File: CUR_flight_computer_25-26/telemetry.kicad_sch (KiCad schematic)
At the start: 8 parts, among them J14 Conn_Coaxial_Small, U5 E22-400M30S

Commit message: finished footprints
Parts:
- J14: footprint Connector_Coxaial_RFSOLUTIONS_CON-SMA-EDGE-S:Connector_Coxaial_RFSOLUTIONS_CON-SMA-EDGE-S -> Connector_Coxaial_RFSOLUTIONS_CON-SMA-EDGE-S:Conn_Coaxial_RFSOLUTIONS_CON-SMA-EDGE-S
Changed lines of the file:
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@@
 			)
 		)
-		(property "Footprint" "Connector_Coxaial_RFSOLUTIONS_CON-SMA-EDGE-S:Connector_Coxaial_RFSOLUTIONS_CON-SMA-EDGE-S"
+		(property "Footprint" "Connector_Coxaial_RFSOLUTIONS_CON-SMA-EDGE-S:Conn_Coaxial_RFSOLUTIONS_CON-SMA-EDGE-S"
 			(at 128.27 45.72 0)
 			(effects

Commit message: most of layout figured out
trouble finding room for power
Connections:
- net +3.3V is gone; now on net +3V3: R7.1
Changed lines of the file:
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@@
+	)
+	(symbol
+		(lib_id "power:+3V3")
+		(at 44.45 52.07 0)
+		(unit 1)
+		(exclude_from_sim no)
+		(in_bom yes)
+		(on_board yes)
+		(dnp no)
+		(fields_autoplaced yes)
+		(property "Reference" "#PWR044"
+			(at 44.45 55.88 0)
+			(effects
+				(font
+					(size 1.27 1.27)
+				)
+				(hide yes)
+			)
+		)
+		(property "Value" "+3V3"
+			(at 44.45 46.99 0)
+			(effects
+				(font
+					(size 1.27 1.27)
+				)
+			)
+		)
+		(property "Footprint" ""
+			(at 44.45 52.07 0)
+			(effects
+				(font
+					(size 1.27 1.27)
+				)
+				(hide yes)
+			)
+		)
+		(property "Datasheet" ""
+			(at 44.45 52.07 0)
+			(effects
+				(font
+					(size 1.27 1.27)
+				)
+				(hide yes)
+			)
+		)
+		(property "Description" "Power symbol creates a global label with name \"+3V3\""
+			(at 44.45 52.07 0)
+			(effects
+				(font
+					(size 1.27 1.27)
+				)
+				(hide yes)
+			)
+		)
+		(pin "1"
+		)
+		(instances
+			(project "CUR_flight_computer_25-26"
+				(path "/bf7761cc-1b32-4d86-809c-5f027005229b/16b7f3d3-745f-44d9-93a4-41f5bfd830cb"
+					(reference "#PWR044")
+					(unit 1)
+				)
+			)
+		)
 	)
 	(symbol
@@
 					(unit 1)
 				)
-			)
-		)
-	)
-	(symbol
-		(lib_id "power:+3.3V")
-		(at 44.45 52.07 0)
-		(unit 1)
-		(exclude_from_sim no)
-		(in_bom yes)
-		(on_board yes)
-		(dnp no)
-		(fields_autoplaced yes)
-		(property "Reference" "#PWR044"
-			(at 44.45 55.88 0)
-			(effects
-				(font
-					(size 1.27 1.27)
-				)
-				(hide yes)
-			)
-		)
-		(property "Value" "+3.3V"
-			(at 44.45 46.99 0)
-			(effects
-				(font
-					(size 1.27 1.27)
-				)
-			)
-		)
-		(property "Footprint" ""
-			(at 44.45 52.07 0)
-			(effects
-				(font
-					(size 1.27 1.27)
-				)
-				(hide yes)
-			)
-		)
-		(property "Datasheet" ""
-			(at 44.45 52.07 0)
-			(effects
-				(font
-					(size 1.27 1.27)
-				)
-				(hide yes)
-			)
-		)
-		(property "Description" "Power symbol creates a global label with name \"+3.3V\""
-			(at 44.45 52.07 0)
-			(effects
-				(font
-					(size 1.27 1.27)
-				)
-				(hide yes)
-			)
-		)
-		(pin "1"
-		)
-		(instances
-			(project "CUR_flight_computer_25-26"
-				(path "/bf7761cc-1b32-4d86-809c-5f027005229b/16b7f3d3-745f-44d9-93a4-41f5bfd830cb"
-					(reference "#PWR044")
-					(unit 1)
-				)

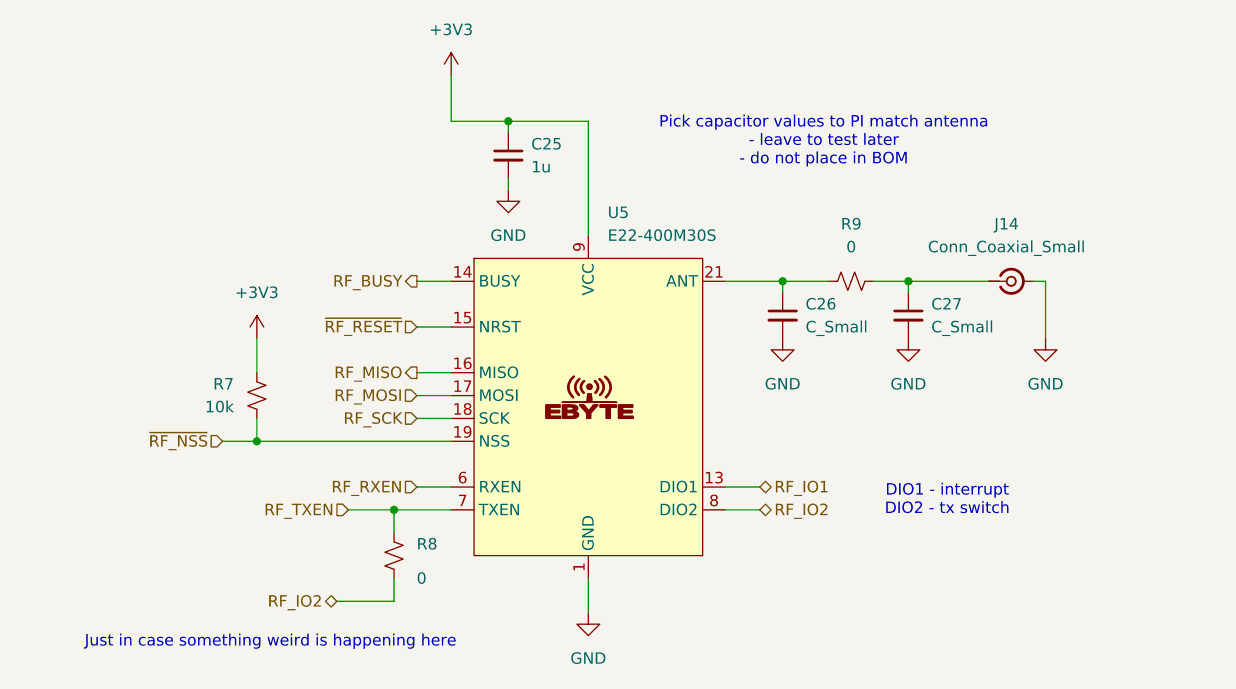
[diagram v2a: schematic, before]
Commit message: added testpoints to schematic
need to update layout
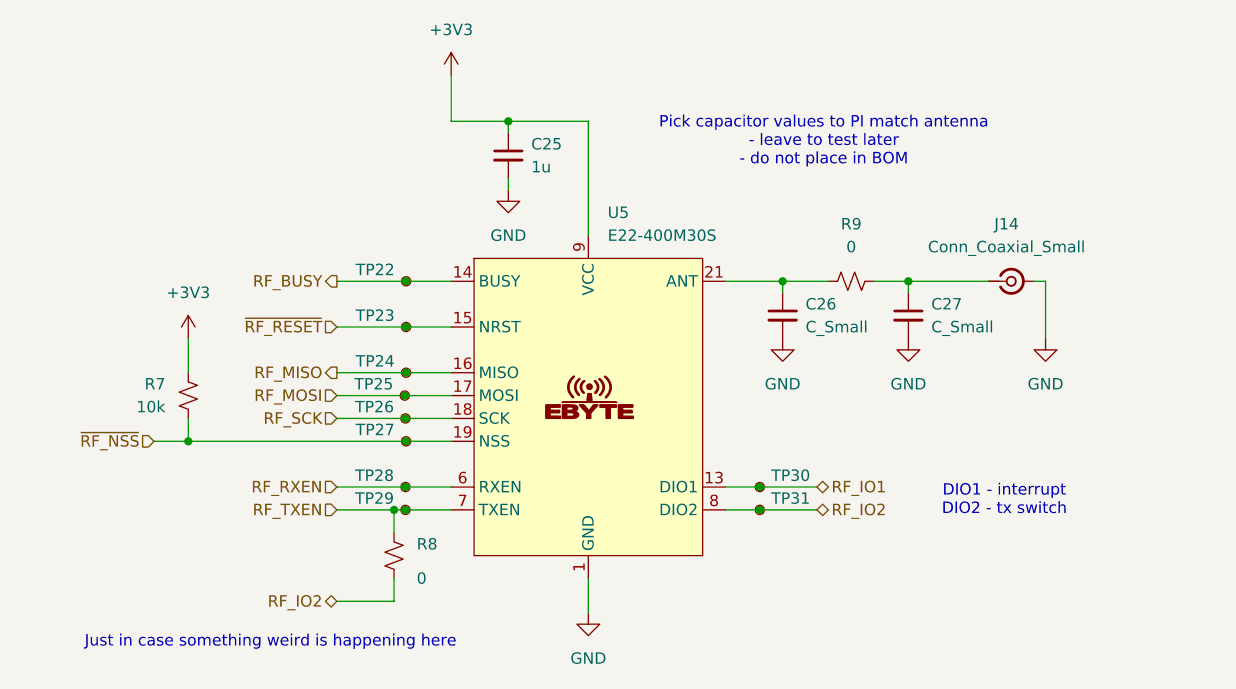
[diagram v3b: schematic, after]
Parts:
- added TP22, TP23, TP24, TP25, TP26, TP27, TP28, TP29, TP30, TP31: TestPoint_Small, TestPoint_KOASpeer:TestPoint_Chip_RCUCTE_0603, symbol Connector:TestPoint_Small
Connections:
- net RF_BUSY: now also TP22.1
- net RF_IO1: now also TP30.1
- net RF_IO2: now also TP31.1
- net RF_MISO: now also TP24.1
- net RF_MOSI: now also TP25.1
- net RF_RXEN: now also TP28.1
- net RF_SCK: now also TP26.1
- net RF_TXEN: now also TP29.1
- net ~{RF_NSS}: now also TP27.1
- net ~{RF_RESET}: now also TP23.1
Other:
- moved on the sheet: R7

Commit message: updated rf module to ebyte-lora-400MM-22s
added footprint
added symbol
updates schematic
updated pcb
need to reroute
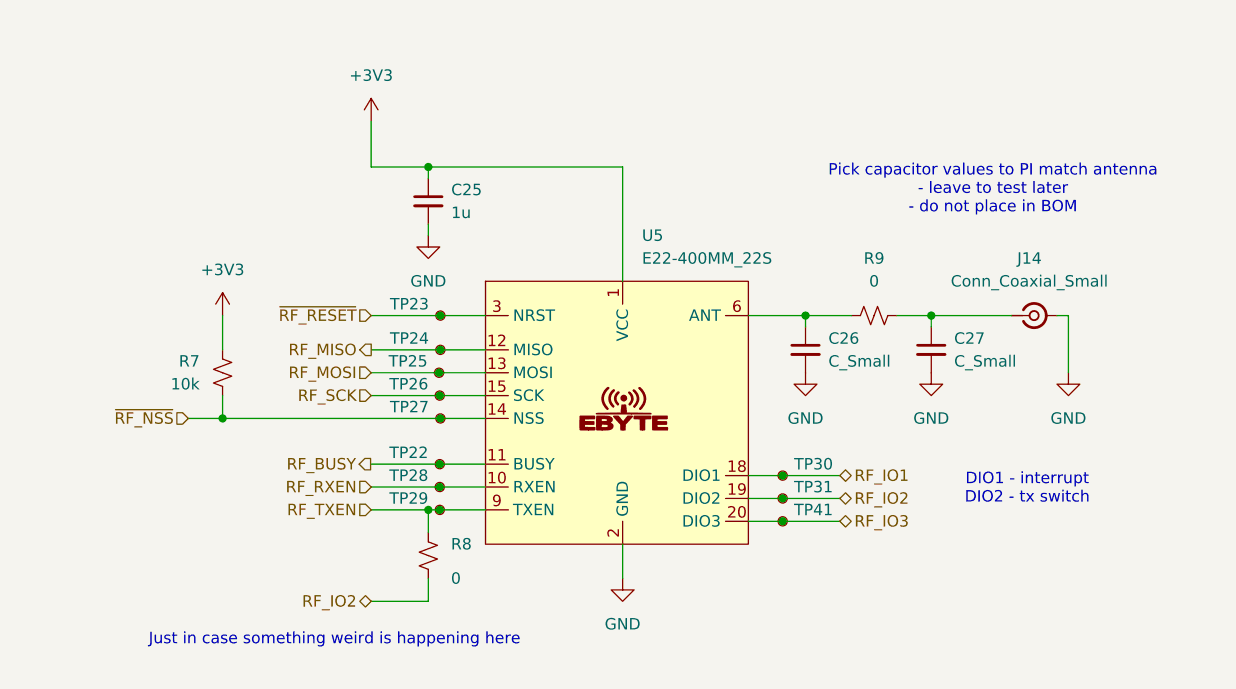
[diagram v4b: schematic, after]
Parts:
- removed U5: E22-400M30S, EBYTE_LoRa:EBYTE_LoRa_E22-400M30S, symbol EBYTE_LoRa:EBYTE_LoRa_E22-400M30S
- added TP41: TestPoint_Small, TestPoint_KOASpeer:TestPoint_Chip_RCUCTE_0603, symbol Connector:TestPoint_Small
- added U5: E22-400MM_22S, EBYTE_LoRa:EBYTE_LoRA_E22-400MM22S, symbol EBYTE_LoRa:EBYTE_LoRa_E22-400MM22S
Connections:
- net +3V3: now also U5.1 (VCC)
- net GND: now also U5.16 (GND), U5.2 (GND), U5.7 (GND)
- net RF_IO1: now also U5.18 (DIO1)
- net RF_IO2: now also U5.19 (DIO2)
- net RF_MISO: now also U5.12 (MISO)
- net RF_MOSI: now also U5.13 (MOSI)
- net RF_RXEN: now also U5.10 (RXEN)
- net RF_SCK: now also U5.15 (SCK)
- net RF_TXEN: now also U5.9 (TXEN)
- net ~{RF_NSS}: now also U5.14 (NSS)
- net ~{RF_RESET}: now also U5.3 (NRST)
- net at C26.1, R9.2: now also U5.6 (ANT)
- new net RF_IO3: TP41.1, U5.20 (DIO3)
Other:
- moved on the sheet: C25, C26, C27, J14, R7, R8, R9, TP22, TP23, TP24, TP25, TP26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

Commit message: Update telemetry.kicad_sch
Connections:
- net RF_BUSY: now also U5.11 (BUSY)
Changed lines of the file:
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@@
 	(wire
 		(pts
-			(xy 64.77 66.04) (xy 69.7821 66.04)
+			(xy 64.77 66.04) (xy 69.85 66.04)
 		)
 		(stroke
